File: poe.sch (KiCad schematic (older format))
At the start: 68 parts, among them J301 PJ-102AH, J302 PJ-102AH, J303 Conn_01x02, J304 Conn_01x02, Q201 FDT86244, Q301 DMMT5401, Q302 DMMT5401, T201 HR051067, U201 TPS23753A, U202 TL431A, U203 EL3H7A

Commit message: PoE layout
Changed opto and fixed ref diode footprint/symbol
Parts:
- U202: symbol Reference_Voltage:TL431D -> Reference_Voltage:TL431DBZ
- U203: value EL3H7A -> TCMT1107; footprint (none) -> Package_SO:SOIC-4_4.55x2.6mm_P1.27mm; Digikey (none) -> TCMT1107CT-ND; LCSC C181879 -> C81148; MPN EL3H7(A)(TA)-G -> TCMT1107; Note (none) -> Optoisolator Transistor Output 3750Vrms 1 Channel 4-SOP
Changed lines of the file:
@@
 $EndComp
 $Comp
-L Reference_Voltage:TL431D U?
+L Reference_Voltage:TL431DBZ U?
 U 1 1 5F85964F
 P 11850 7100
@@
 AR Path="/5FCEDB09/5FAC6B33/5F859657" Ref="U4"  Part="1"
 F 0 "U4" H 10300 8025 50  0000 C CNN
-F 1 "EL3H7A" H 10300 7934 50  0000 C CNN
-F 2 "" H 10100 7500 50  0001 L CIN
-F 3 "" H 10300 7700 50  0001 L CNN
-F 4 "EL3H7(A)(TA)-G" H 10300 7700 50  0001 C CNN "MPN"
-F 5 "C181879" H 10300 7700 50  0001 C CNN "LCSC"
+F 1 "TCMT1107" H 10300 7934 50  0000 C CNN
+F 2 "Package_SO:SOIC-4_4.55x2.6mm_P1.27mm" H 10100 7500 50  0001 L CIN
+F 3 "https://www.vishay.com/docs/83510/tcmt1100.pdf" H 10300 7700 50  0001 L CNN
+F 4 "TCMT1107" H 10300 7700 50  0001 C CNN "MPN"
+F 5 "C81148" H 10300 7700 50  0001 C CNN "LCSC"
+F 6 "TCMT1107CT-ND" H 10300 7700 50  0001 C CNN "Digikey"
+F 7 "Optoisolator Transistor Output 3750Vrms 1 Channel 4-SOP" H 10300 7700 50  0001 C CNN "Note"
 	1    10300 7700
 	-1   0    0    -1

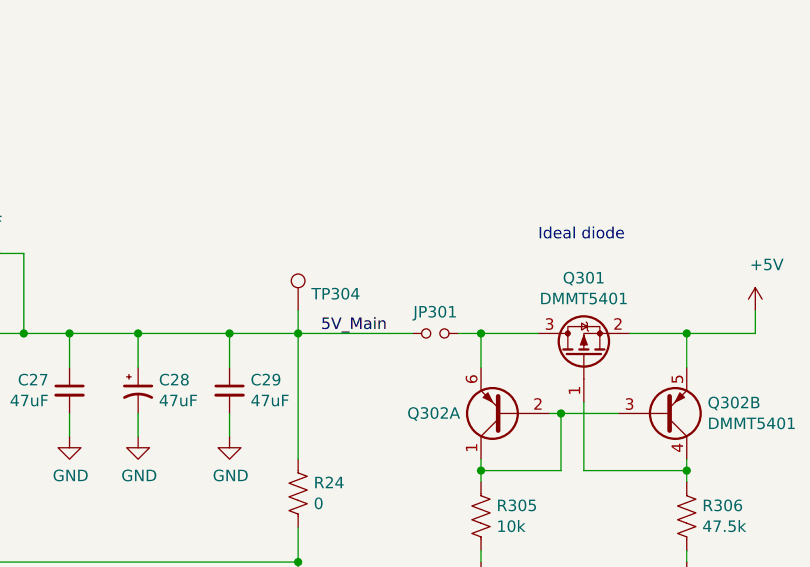
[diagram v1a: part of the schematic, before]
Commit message: Added battery charger schematic
Annotated
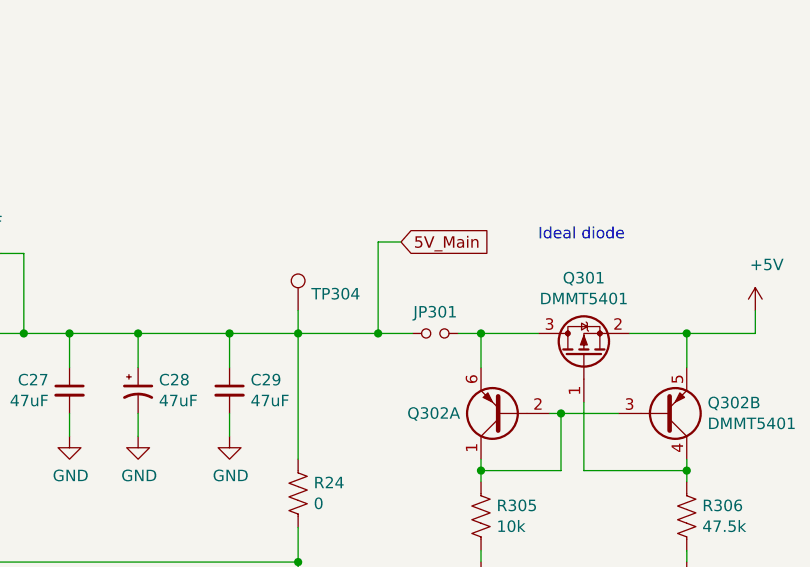
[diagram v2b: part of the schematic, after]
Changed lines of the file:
@@
 	14750 4950 14450 4950
 Connection ~ 14450 4950
-Text Label 12850 4950 0    50   ~ 0
-5V_Main
 Text Label 14850 6750 2    50   ~ 0
 5V_Main
@@
 Connection ~ 13550 4950
 Wire Wire Line
-	13250 4950 12750 4950
+	13250 4950 13100 4950
+Text GLabel 13200 4550 2    50   Input ~ 0
+5V_Main
+Wire Wire Line
+	13200 4550 13100 4550
+Wire Wire Line
+	13100 4550 13100 4950
+Connection ~ 13100 4950
+Wire Wire Line
+	13100 4950 12750 4950
 $EndSCHEMATC

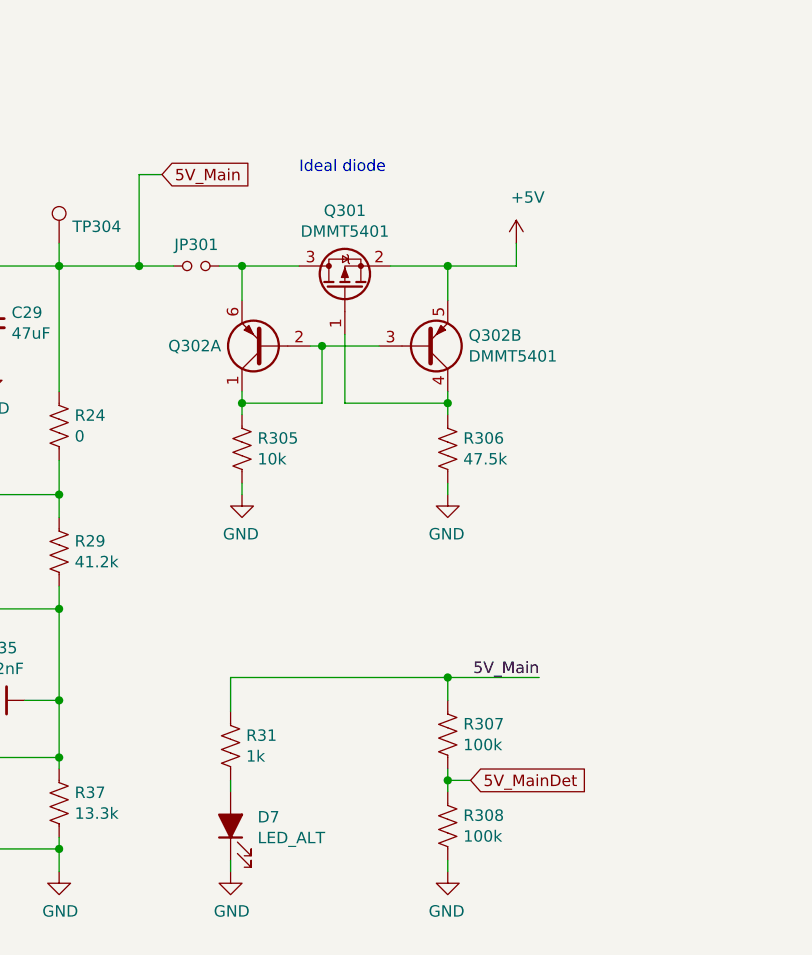
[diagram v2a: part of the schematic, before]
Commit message: Cleaned up, Annotated
Added Global 5V_Main net, solder jumper for battery charger, jumper for speaker and speaker_alt, added parts for battery charger
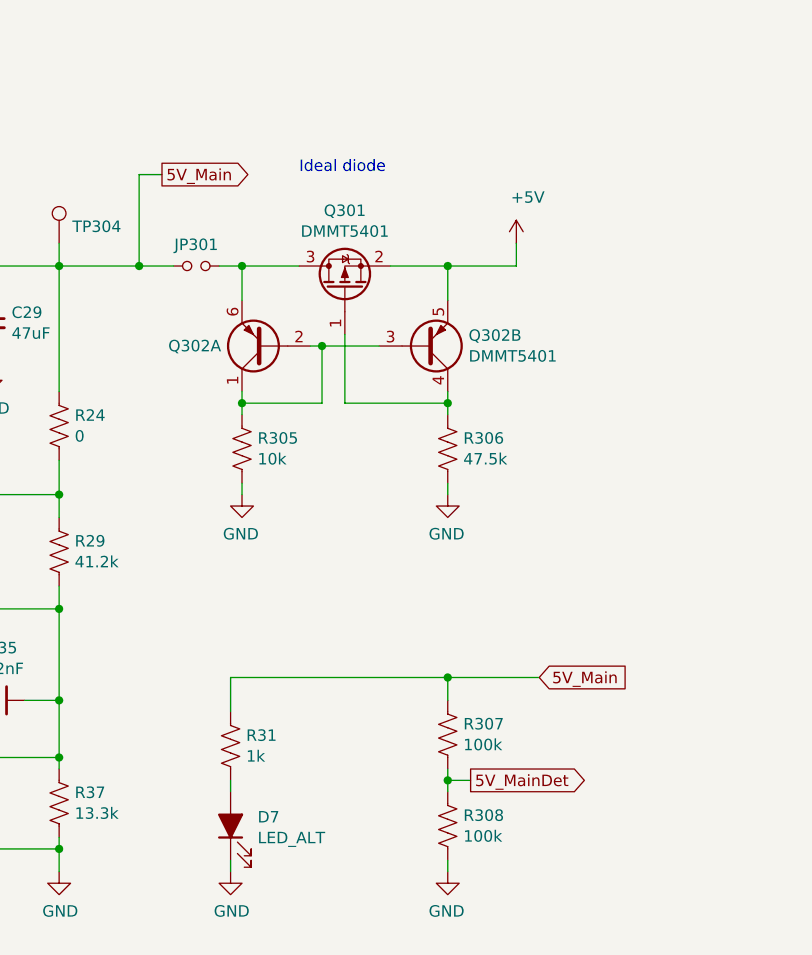
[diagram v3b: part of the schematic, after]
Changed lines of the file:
@@
 	14750 4950 14450 4950
 Connection ~ 14450 4950
-Text Label 14850 6750 2    50   ~ 0
-5V_Main
 $Comp
 L Connector:TestPoint TP304
@@
 Wire Wire Line
 	14450 7250 14450 7200
-Text GLabel 14550 7200 2    50   Input ~ 0
+Text GLabel 14550 7200 2    50   Output ~ 0
 5V_MainDet
 Wire Wire Line
@@
 Wire Wire Line
 	13250 4950 13100 4950
-Text GLabel 13200 4550 2    50   Input ~ 0
+Text GLabel 13200 4550 2    50   Output ~ 0
 5V_Main
 Wire Wire Line
@@
 Wire Wire Line
 	13100 4950 12750 4950
+Text GLabel 14850 6750 2    50   Input ~ 0
+5V_Main
 $EndSCHEMATC

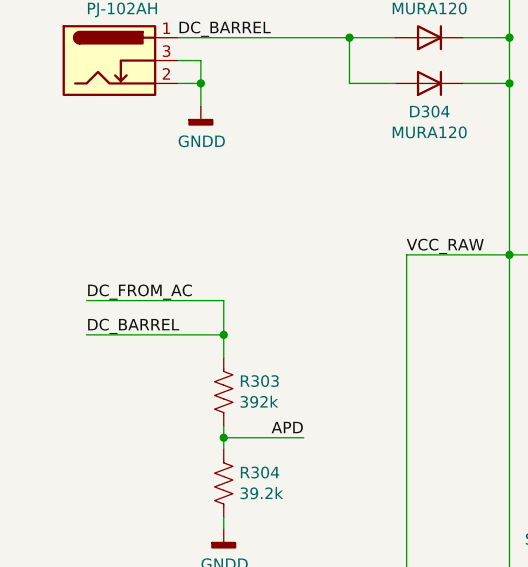
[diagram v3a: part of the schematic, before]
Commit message: Add diodes to seperate APD
Previously the APD feedback network directly shorted DC_FROM_AC and DC_BARREL together.
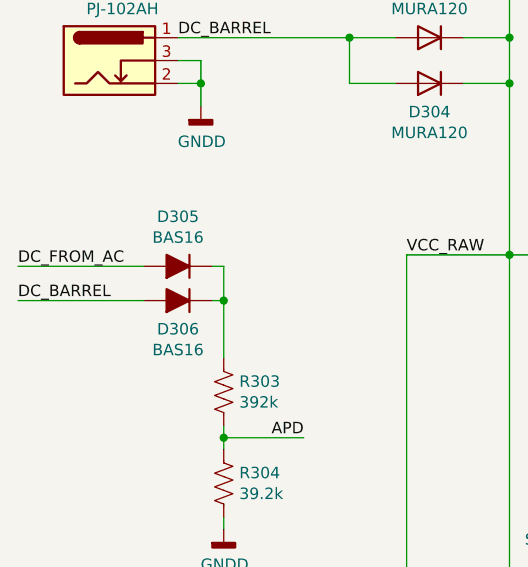
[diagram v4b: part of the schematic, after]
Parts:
- added D305, D306: BAS16, Diode_SMD:D_SOT-23_ANK, symbol Device:D_ALT
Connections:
- net DC_BARREL: now also D306.2 (A); no longer D301.2 (A), D302.2 (A), J301.1, R303.1
- new net: D305.1 (K), D306.1 (K), R303.1
- new net DC_FROM_AC: D301.2 (A), D302.2 (A), D305.2 (A), J301.1
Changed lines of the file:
@@
 	-1   0    0    1
 $EndComp
-Text Label 2350 4450 0    50   ~ 0
+Text Label 2050 4300 0    50   ~ 0
 DC_FROM_AC
-Text Label 2350 4600 0    50   ~ 0
+Text Label 2050 4450 0    50   ~ 0
 DC_BARREL
 Connection ~ 2950 5050
@@
 $EndComp
 Wire Wire Line
-	2950 4700 2950 4600
-Wire Wire Line
-	2950 4600 2350 4600
-Wire Wire Line
-	2350 4450 2950 4450
-Wire Wire Line
-	2950 4450 2950 4600
-Connection ~ 2950 4600
+	2950 4700 2950 4450
+Wire Wire Line
+	2950 4450 2900 4450
+Wire Wire Line
+	2050 4300 2600 4300
+Wire Wire Line
+	2950 4300 2950 4450
+Connection ~ 2950 4450
 Wire Wire Line
 	2750 3300 3500 3300
@@
 Text GLabel 14850 6750 2    50   Input ~ 0
 5V_Main
+$Comp
+L Device:D_ALT D?
+U 1 1 5FC9A02F
+P 2750 4300
+AR Path="/5F81C554/5FC9A02F" Ref="D?"  Part="1"
+AR Path="/5F9D72A5/5FA9FFA2/5FC9A02F" Ref="D?"  Part="1"
+AR Path="/5FAC6B33/5FC9A02F" Ref="D?"  Part="1"
+AR Path="/5FCEDB09/5FAC6B33/5FC9A02F" Ref="D305"  Part="1"
+F 0 "D305" H 2750 4083 50  0000 C CNN
+F 1 "BAS16" H 2750 4174 50  0000 C CNN
+F 2 "Diode_SMD:D_SOT-23_ANK" H 2750 4300 50  0001 C CNN
+F 3 "~" H 2750 4300 50  0001 C CNN
+F 4 "150mA" H 2750 4300 50  0001 C CNN "Current"
+F 5 "350mW" H 2750 4300 50  0001 C CNN "Power"
+F 6 "75V" H 2750 4300 50  0001 C CNN "Volt"
+F 7 "BAS16-FDICT-ND" H 2750 4300 50  0001 C CNN "Digikey"
+F 8 "C69162*" H 2750 4300 50  0001 C CNN "LCSC"
+F 9 "BAS16-7-F" H 2750 4300 50  0001 C CNN "MPN"
+F 10 "DIODE GEN PURP 75V 200MA SOT23-3" H 2750 4300 50  0001 C CNN "Note"
+	1    2750 4300
+	-1   0    0    1
+$EndComp
+Wire Wire Line
+	2900 4300 2950 4300
+$Comp
+L Device:D_ALT D?
+U 1 1 5FCAB4CB
+P 2750 4450
+AR Path="/5F81C554/5FCAB4CB" Ref="D?"  Part="1"
+AR Path="/5F9D72A5/5FA9FFA2/5FCAB4CB" Ref="D?"  Part="1"
+AR Path="/5FAC6B33/5FCAB4CB" Ref="D?"  Part="1"
+AR Path="/5FCEDB09/5FAC6B33/5FCAB4CB" Ref="D306"  Part="1"
+F 0 "D306" H 2750 4575 50  0000 C CNN
+F 1 "BAS16" H 2750 4666 50  0000 C CNN
+F 2 "Diode_SMD:D_SOT-23_ANK" H 2750 4450 50  0001 C CNN
+F 3 "~" H 2750 4450 50  0001 C CNN
+F 4 "150mA" H 2750 4450 50  0001 C CNN "Current"
+F 5 "350mW" H 2750 4450 50  0001 C CNN "Power"
+F 6 "75V" H 2750 4450 50  0001 C CNN "Volt"
+F 7 "BAS16-FDICT-ND" H 2750 4450 50  0001 C CNN "Digikey"
+F 8 "C69162*" H 2750 4450 50  0001 C CNN "LCSC"
+F 9 "BAS16-7-F" H 2750 4450 50  0001 C CNN "MPN"
+F 10 "DIODE GEN PURP 75V 200MA SOT23-3" H 2750 4450 50  0001 C CNN "Note"
+	1    2750 4450
+	-1   0    0    1
+$EndComp
+Wire Wire Line
+	2600 4450 2050 4450
 $EndSCHEMATC

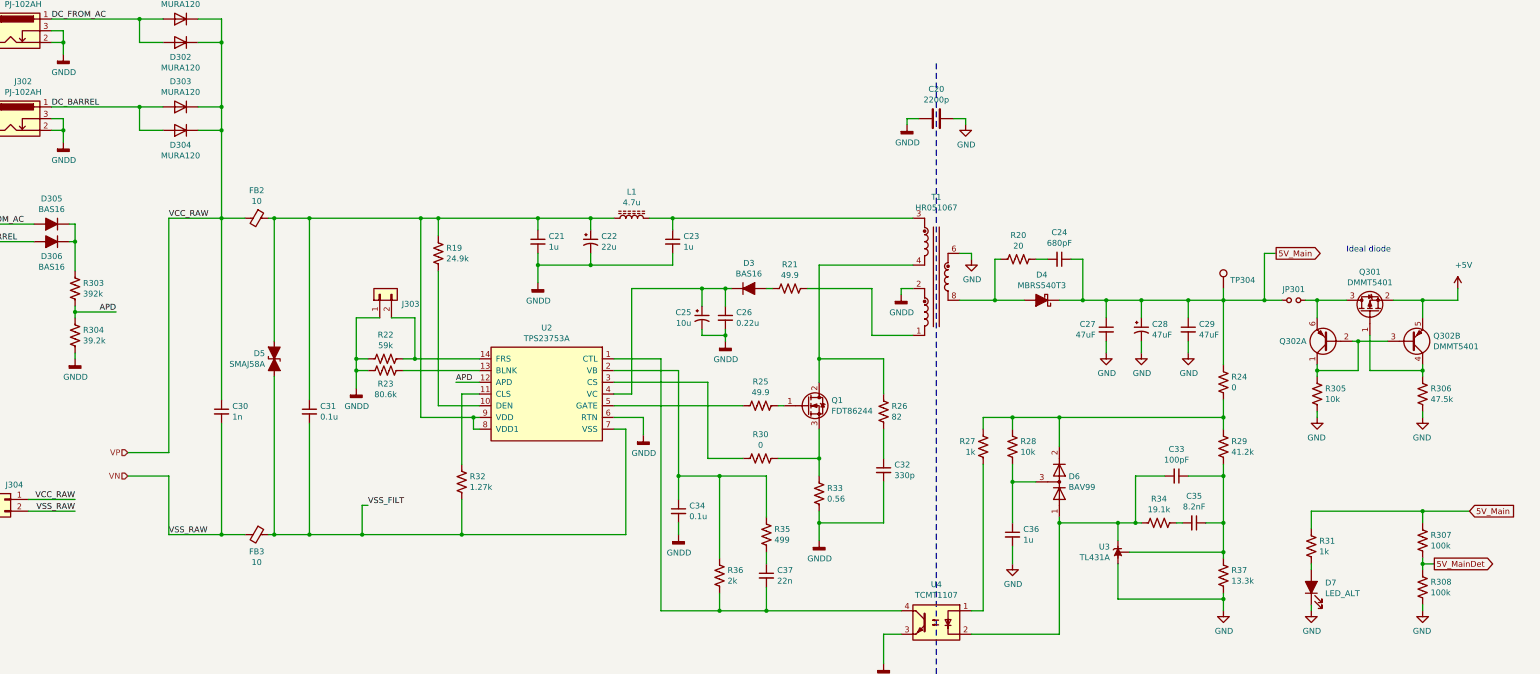
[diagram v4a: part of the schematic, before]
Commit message: Re-annotate all parts
Cleans up annotations
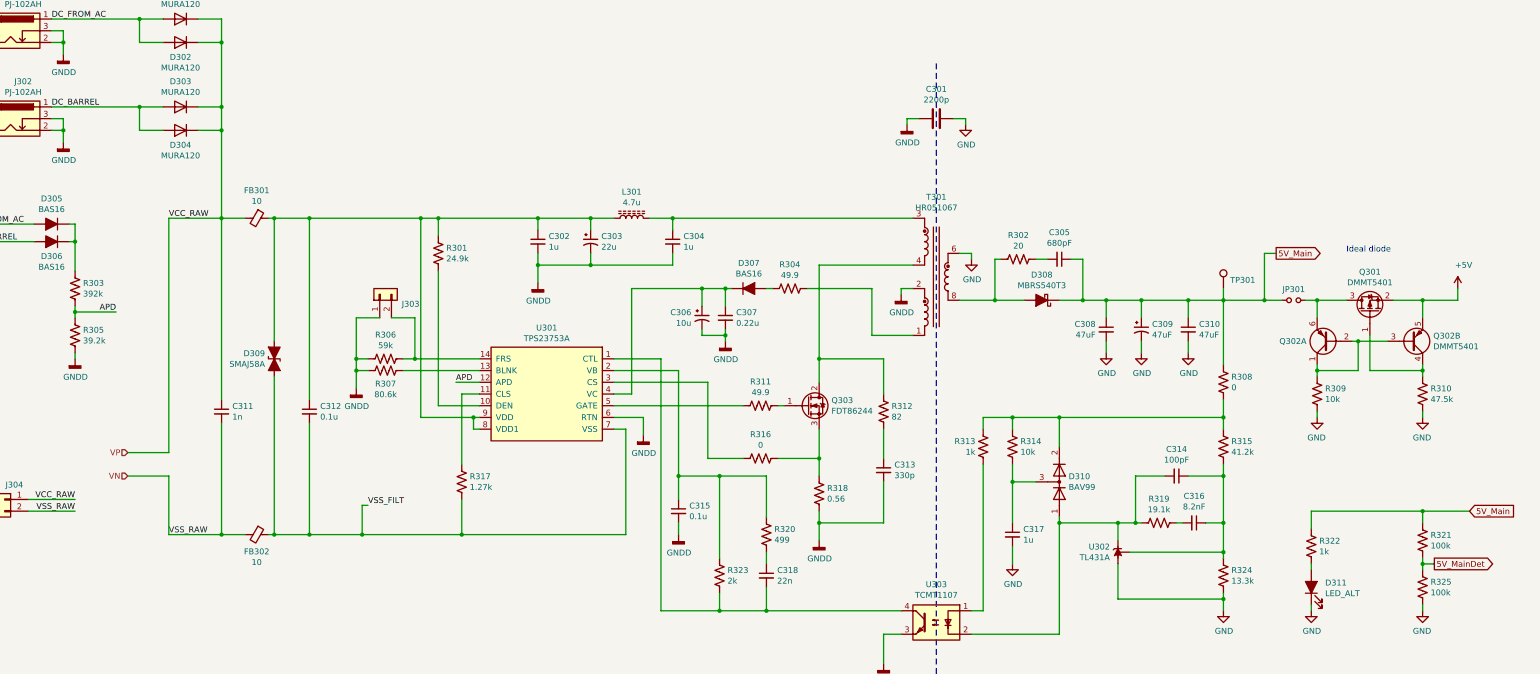
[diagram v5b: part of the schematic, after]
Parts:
- renumbered C201 to C301, C202 to C302, C203 to C303, C204 to C304, C205 to C305, C206 to C306, C207 to C307, C208 to C308, C209 to C309, C210 to C310, C211 to C311, C212 to C312, C213 to C313, C214 to C314, C215 to C315, C216 to C316, C217 to C317, C218 to C318, D203 to D307, D204 to D308, D205 to D309, D206 to D310, D207 to D311, FB201 to FB301, FB202 to FB302, L201 to L301, Q201 to Q303, R203 to R301, R204 to R302, R205 to R304, R304 to R305, R206 to R306, R207 to R307, R208 to R308, R305 to R309, R306 to R310, R209 to R311, R210 to R312, R211 to R313, R212 to R314, R213 to R315, R214 to R316, R216 to R317, R217 to R318, R218 to R319, R219 to R320, R307 to R321, R215 to R322, R220 to R323, R221 to R324, R308 to R325, T201 to T301, TP304 to TP301, U201 to U301, U202 to U302, U203 to U303

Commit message: Prefinal, layout done
Update FB to use inductor footprints
DNP net tie
Update diode symbol in power
Add battery voltage divider in power
Supply 5V power to aux sensor connector
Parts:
- FB301, FB302: footprint Resistor_SMD:R_0603_1608Metric -> Inductor_SMD:L_0603_1608Metric
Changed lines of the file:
@@
 F 0 "FB301" V 4263 4250 50  0000 C CNN
 F 1 "10" V 4354 4250 50  0000 C CNN
-F 2 "Resistor_SMD:R_0603_1608Metric" V 4430 4250 50  0001 C CNN
+F 2 "Inductor_SMD:L_0603_1608Metric" V 4430 4250 50  0001 C CNN
 F 3 "~" H 4500 4250 50  0001 C CNN
 F 4 "MMZ2012R150AT000" V 4500 4250 50  0001 C CNN "Mfr"
@@
 F 0 "FB302" V 4645 6950 50  0000 C CNN
 F 1 "10" V 4736 6950 50  0000 C CNN
-F 2 "Resistor_SMD:R_0603_1608Metric" V 4430 6950 50  0001 C CNN
+F 2 "Inductor_SMD:L_0603_1608Metric" V 4430 6950 50  0001 C CNN
 F 3 "~" H 4500 6950 50  0001 C CNN
 F 4 "MMZ2012R150AT000" V 4500 6950 50  0001 C CNN "Mfr"
